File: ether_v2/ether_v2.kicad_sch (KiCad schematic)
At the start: 82 parts, among them J1 CV A1, J10 CV B5, J11 CV A6, J12 CV B6, J13 CV A7, J14 CV B7, J15 CV A8, J16 CV B8, J17 Ethernet A, J18 Ethernet B, J2 CV B1, J20 Conn_01x03, J3 CV A2, J4 CV B2, J5 CV A3, J6 CV B3, J7 CV A4, J8 CV B4, J9 CV A5, J99 Power, U1 TL074, U2 TL074, U3 TL074, U4 TL074

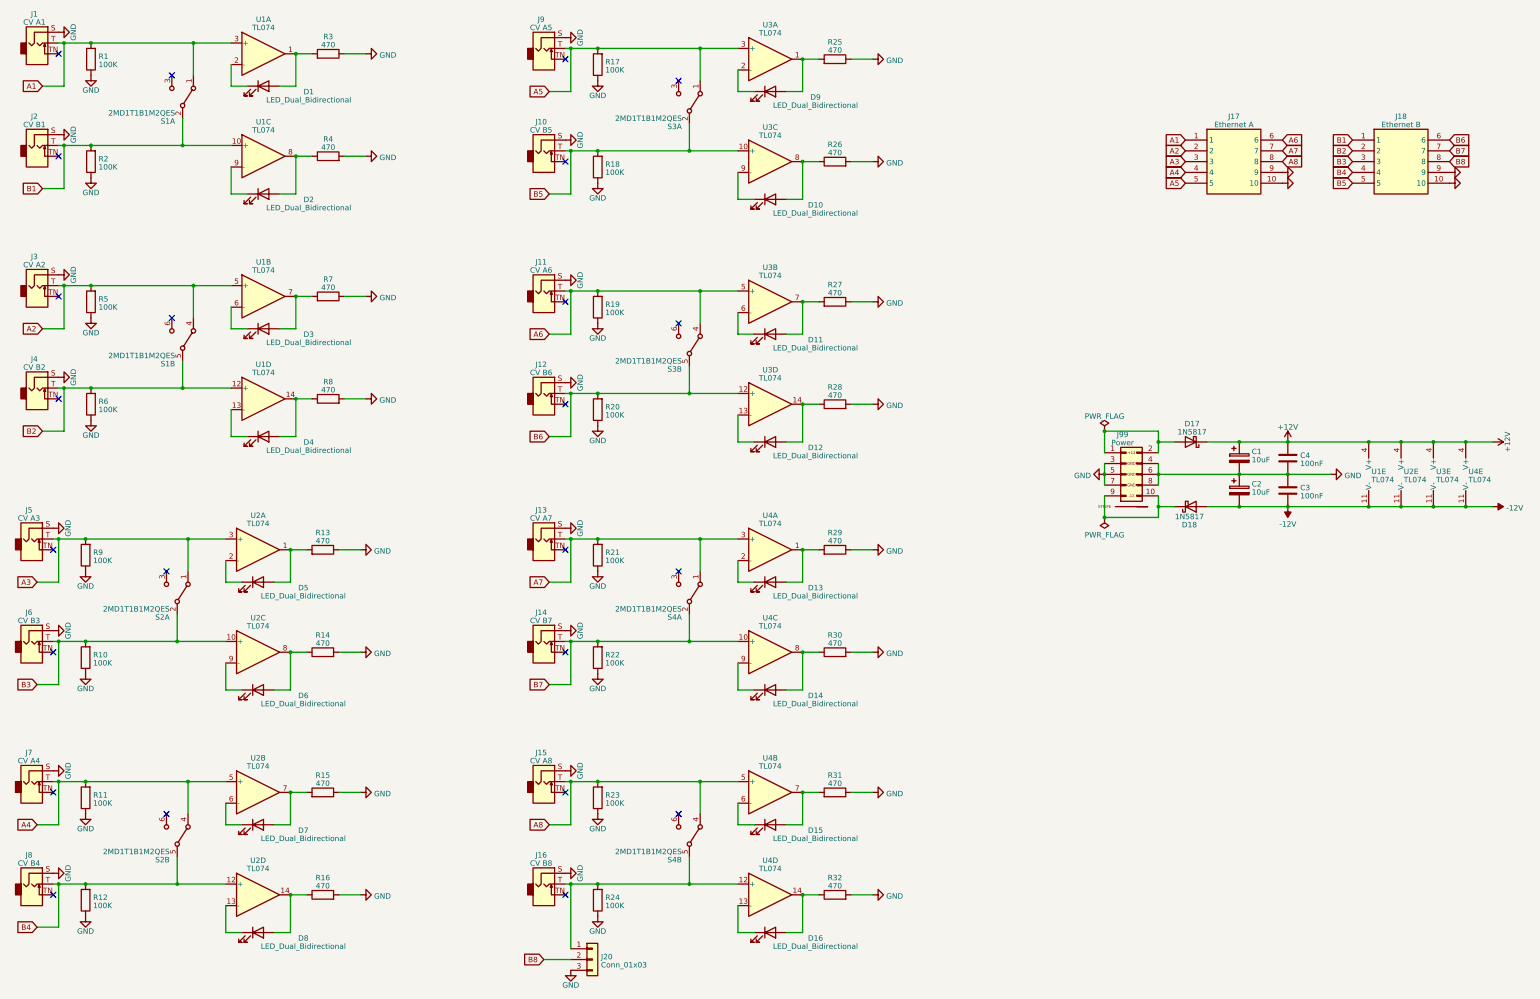
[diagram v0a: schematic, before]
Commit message: Add Ether Twin v1 README, bom, schematic.
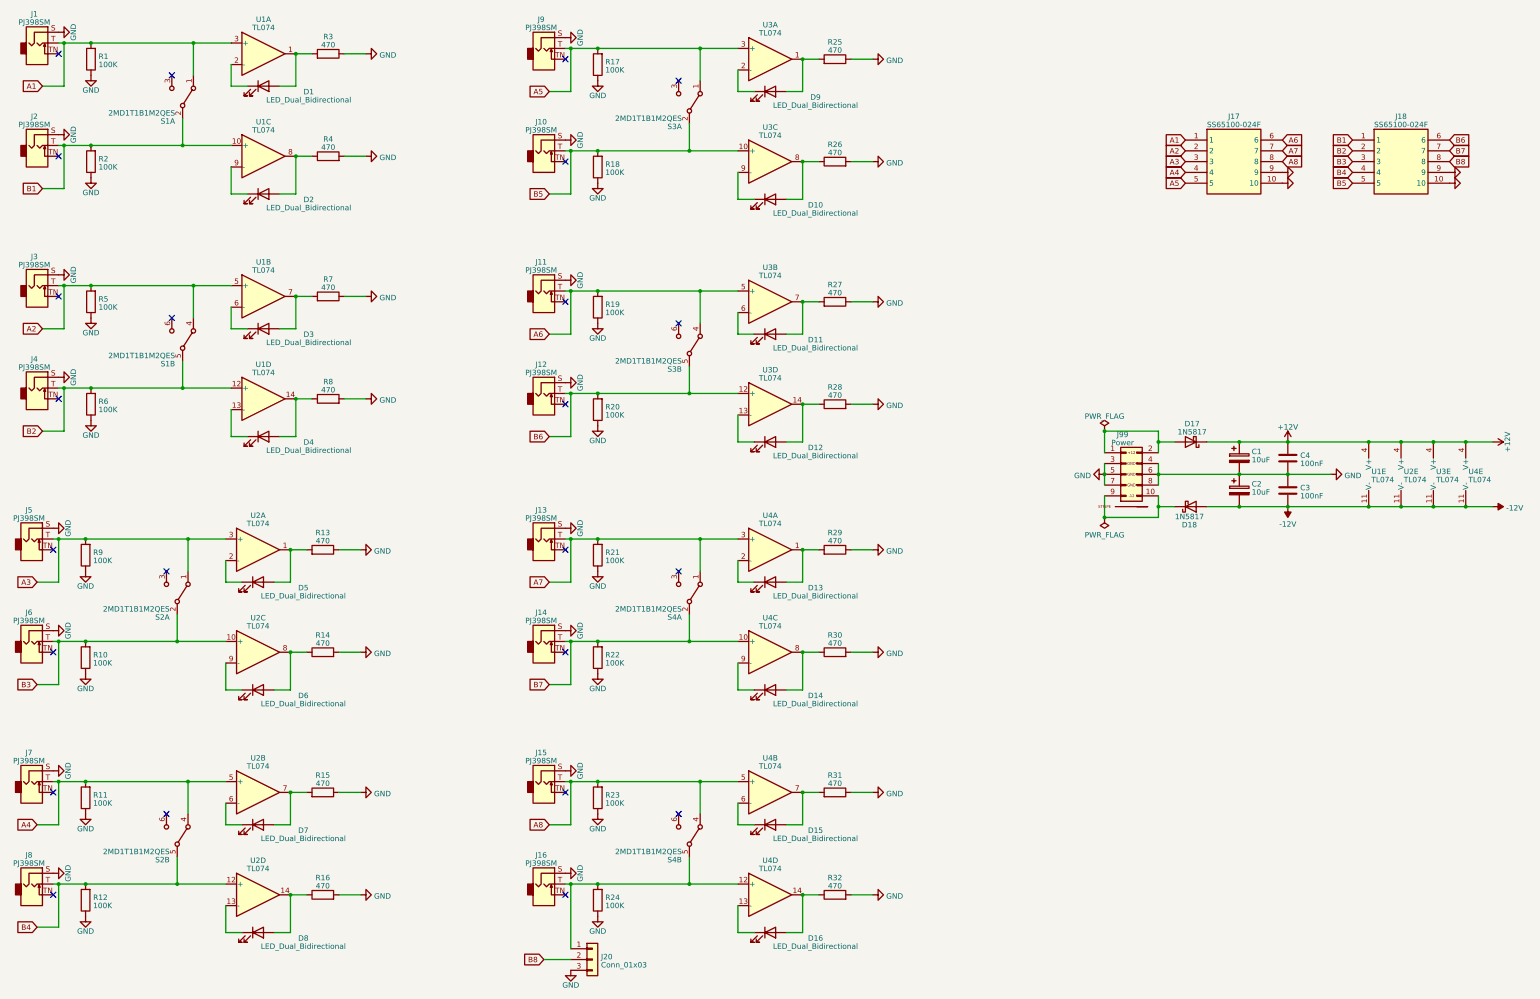
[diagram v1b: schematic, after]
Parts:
- D17, D18: LCSC (none) -> C727113
- J1: value CV A1 -> PJ398SM
- J10: value CV B5 -> PJ398SM
- J11: value CV A6 -> PJ398SM
- J12: value CV B6 -> PJ398SM
- J13: value CV A7 -> PJ398SM
- J14: value CV B7 -> PJ398SM
- J15: value CV A8 -> PJ398SM
- J16: value CV B8 -> PJ398SM
- J17: value Ethernet A -> SS65100-024F
- J18: value Ethernet B -> SS65100-024F
- J2: value CV B1 -> PJ398SM
- J3: value CV A2 -> PJ398SM
- J4: value CV B2 -> PJ398SM
- J5: value CV A3 -> PJ398SM
- J6: value CV B3 -> PJ398SM
- J7: value CV A4 -> PJ398SM
- J8: value CV B4 -> PJ398SM
- J9: value CV A5 -> PJ398SM

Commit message: Fix incorrect placement of ground and led resistor. Fixes Odd wiring of LED in schematic. #1
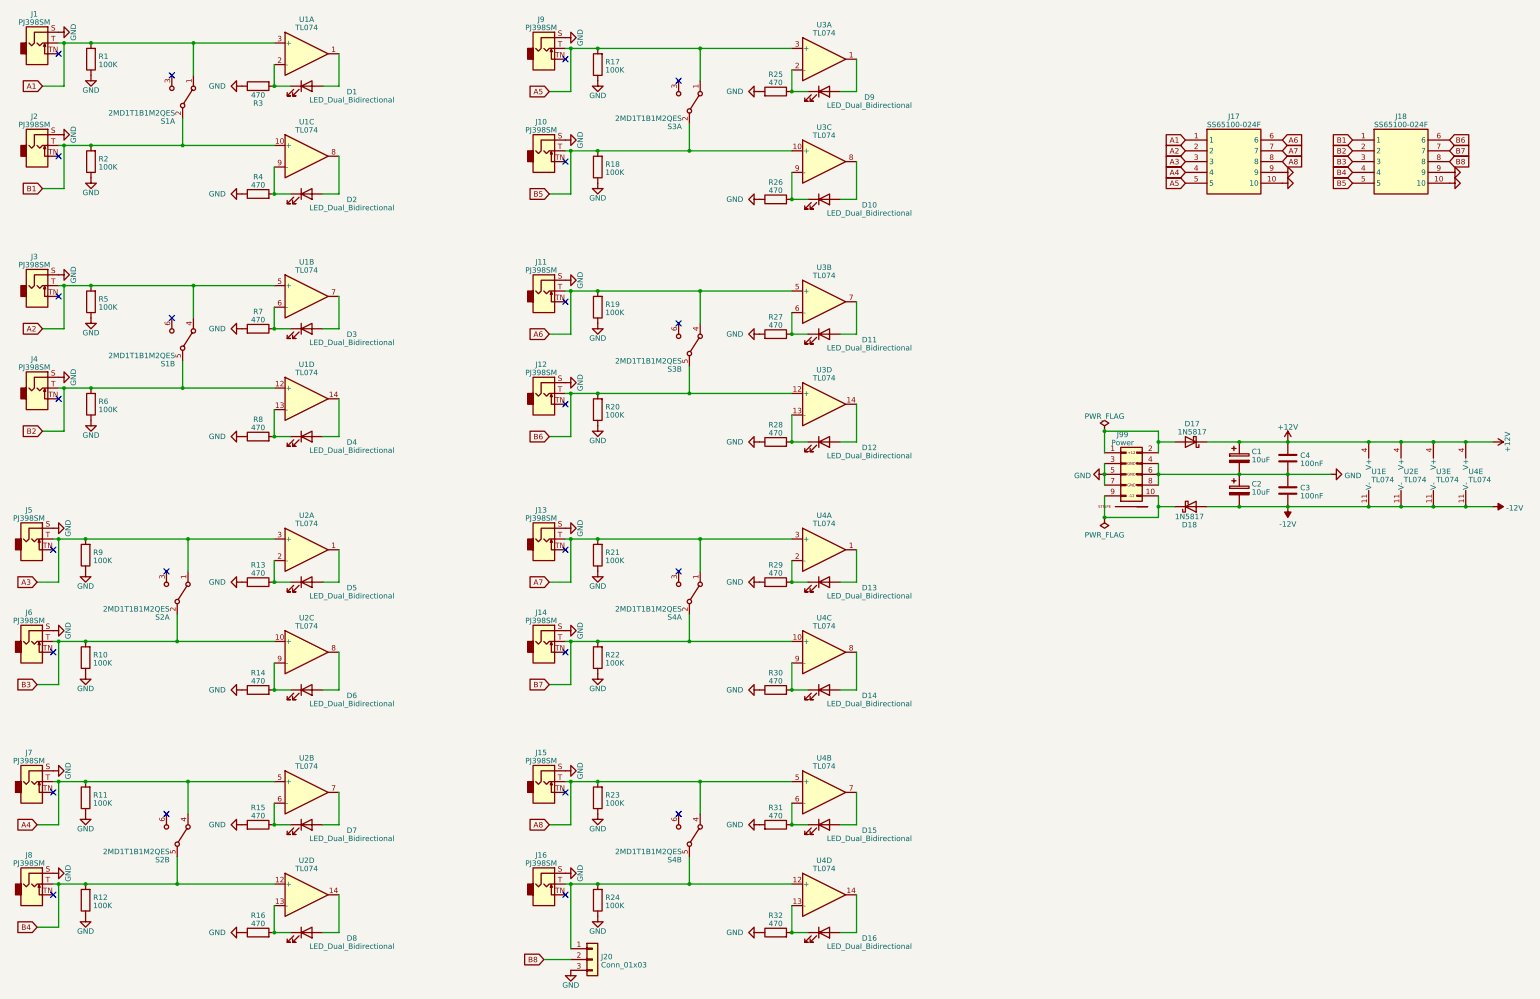
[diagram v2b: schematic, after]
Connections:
- net GND: now also R13.2, R14.1, R15.2, R16.1, R25.2, R26.1, R27.2, R28.1, R29.2, R30.1, R31.2, R32.1, R4.1, R7.2, R8.1; no longer R13.1, R14.2, R15.1, R16.2, R25.1, R26.2, R27.1, R28.2, R29.1, R30.2, R31.1, R32.2, R4.2, R7.1, R8.2
- net at D15.1 (K), U4.6 (-): now also R31.1
- net at D15.2 (A), U4.7: no longer R31.2
- net at D5.2 (A), U2.1: no longer R13.2
- net at D8.1 (K), U2.13 (-): now also R16.2
- net at D8.2 (A), U2.14: no longer R16.1
- net at D9.2 (A), U3.1: no longer R25.2
- net at D10.2 (A), U3.8: no longer R26.1
- net at D7.1 (K), U2.6 (-): now also R15.1
- net at D7.2 (A), U2.7: no longer R15.2
- net at D14.2 (A), U4.8: no longer R30.1
- net at D14.1 (K), U4.9 (-): now also R30.2
- net at D1.2 (A), U1.1: no longer R3.2
- net at D1.1 (K), U1.2 (-): now also R3.2
- net at D10.1 (K), U3.9 (-): now also R26.2
- net at D2.2 (A), U1.8: no longer R4.1
- net at D12.2 (A), U3.14: no longer R28.1
- net at D3.2 (A), U1.7: no longer R7.2
- net at D11.2 (A), U3.7: no longer R27.2
- net at D4.1 (K), U1.13 (-): now also R8.2
- net at D4.2 (A), U1.14: no longer R8.1
- net at D5.1 (K), U2.2 (-): now also R13.1
- net at D11.1 (K), U3.6 (-): now also R27.1
- net at D2.1 (K), U1.9 (-): now also R4.2
- net at D9.1 (K), U3.2 (-): now also R25.1
- net at D12.1 (K), U3.13 (-): now also R28.2
- net at D13.2 (A), U4.1: no longer R29.2
- net at D6.1 (K), U2.9 (-): now also R14.2
- net at D6.2 (A), U2.8: no longer R14.1
- net at D3.1 (K), U1.6 (-): now also R7.1
- net at D16.1 (K), U4.13 (-): now also R32.2
- net at D16.2 (A), U4.14: no longer R32.1
- net at D13.1 (K), U4.2 (-): now also R29.1
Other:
- moved on the sheet: D1, D10, D11, D12, D13, D14, D15, D16, D2, D3, D4, D5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

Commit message: fix bad merge
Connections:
- net GND: now also R13.1, R14.2, R15.1, R16.2, R25.1, R26.2, R27.1, R28.2, R29.1, R30.2, R31.1, R32.2, R4.2, R7.1, R8.2; no longer R13.2, R14.1, R15.2, R16.1, R25.2, R26.1, R27.2, R28.1, R29.2, R30.1, R31.2, R32.1, R4.1, R7.2, R8.1
- net at D15.1 (K), U4.6 (-): no longer R31.1
- net at D15.2 (A), U4.7: now also R31.2
- net at D8.1 (K), U2.13 (-): no longer R16.2
- net at D8.2 (A), U2.14: now also R16.1
- net at D3.1 (K), U1.6 (-): no longer R7.1
- net at D7.1 (K), U2.6 (-): no longer R15.1
- net at D7.2 (A), U2.7: now also R15.2
- net at D14.2 (A), U4.8: now also R30.1
- net at D14.1 (K), U4.9 (-): no longer R30.2
- net at D1.2 (A), U1.1: now also R3.2
- net at D1.1 (K), U1.2 (-): no longer R3.2
- net at D11.1 (K), U3.6 (-): no longer R27.1
- net at D10.1 (K), U3.9 (-): no longer R26.2
- net at D10.2 (A), U3.8: now also R26.1
- net at D4.1 (K), U1.13 (-): no longer R8.2
- net at D4.2 (A), U1.14: now also R8.1
- net at D5.1 (K), U2.2 (-): no longer R13.1
- net at D5.2 (A), U2.1: now also R13.2
- net at D11.2 (A), U3.7: now also R27.2
- net at D2.1 (K), U1.9 (-): no longer R4.2
- net at D6.1 (K), U2.9 (-): no longer R14.2
- net at D2.2 (A), U1.8: now also R4.1
- net at D9.2 (A), U3.1: now also R25.2
- net at D9.1 (K), U3.2 (-): no longer R25.1
- net at D12.1 (K), U3.13 (-): no longer R28.2
- net at D12.2 (A), U3.14: now also R28.1
- net at D6.2 (A), U2.8: now also R14.1
- net at D3.2 (A), U1.7: now also R7.2
- net at D16.1 (K), U4.13 (-): no longer R32.2
- net at D16.2 (A), U4.14: now also R32.1
- net at D13.1 (K), U4.2 (-): no longer R29.1
- net at D13.2 (A), U4.1: now also R29.2
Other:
- moved on the sheet: D1, D10, D11, D12, D13, D14, D15, D16, D2, D3, D4, D5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
